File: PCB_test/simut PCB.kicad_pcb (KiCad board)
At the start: 2 copper layers, 125 x 102 mm, 49 parts, among them J1 Conn_01x10, J2 Conn_01x10, J3 Conn_01x03, J4 Conn_01x12, J5 Conn_01x14, J6 Conn_01x03, J7 Conn_01x03, Q1 BC337, U2 HLK-PM01

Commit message: Update PCB_test: refresh Gerber fabrication files and KiCad PCB layout
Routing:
- net GND: track 205.8 -> 220.7 mm

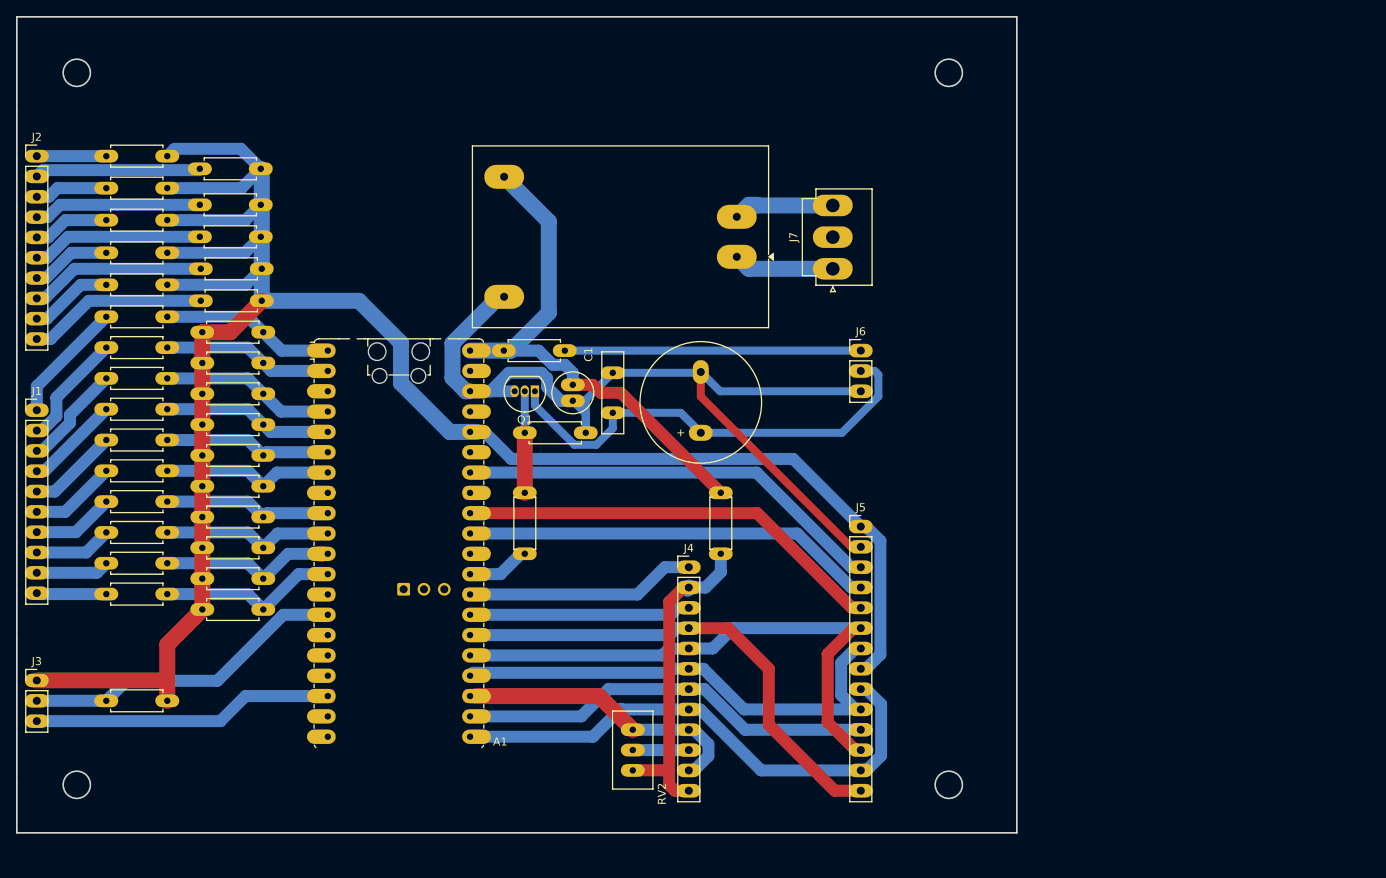
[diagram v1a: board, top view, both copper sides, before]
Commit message: Update PCB_test: correct the alphanumeric display pinout and relabel the board
The alphanumeric display header carried the wrong pinout. This regenerates the
layout and the whole fabrication output from it, so the Gerbers, the drill files
and the zip all come from the same source revision as the .kicad_pcb.

The silkscreen went from three stray numbers to a labelled board: pin names for
the TFT and touch headers, the HD44780 block under an "Alphanumeric" caption,
the sensor column S0 to S10, the mains warning and the project URL. Copper zones
were refilled as a consequence, which is most of the diff size.

The zip carries the ten fabrication files plus the .kicad_pcb source, and every
file in it is byte-identical to its loose copy in this directory.
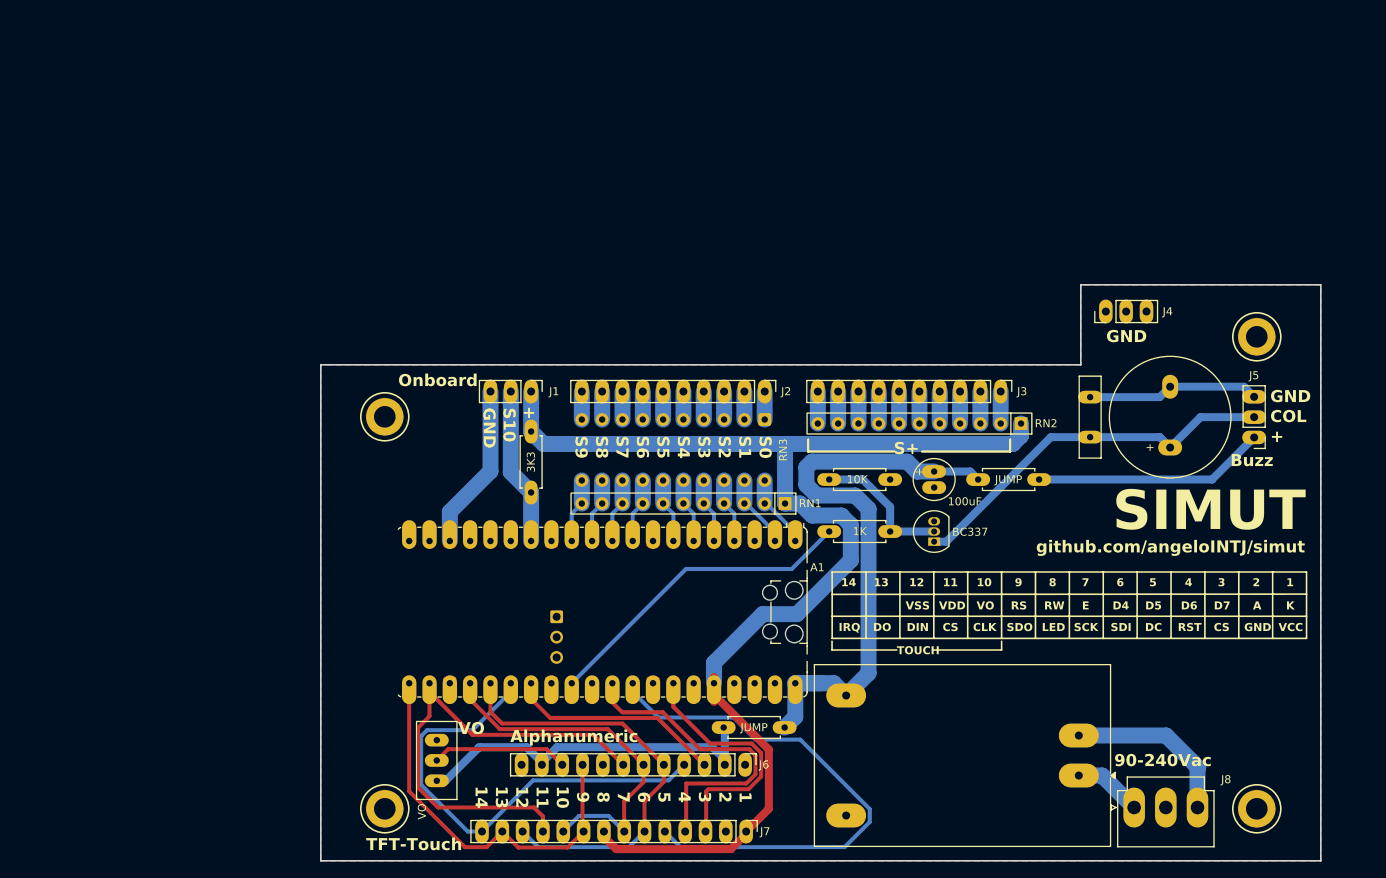
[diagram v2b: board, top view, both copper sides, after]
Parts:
- removed R1, R10, R11, R12, R13, R14, R15, R16, R17, R18, R19, R2, R20, R21, R22, R23, R24, R25, R26, R27, R28, R29, R3, R30, R4, R5, R6, R7, R8, R9: R, Resistor_THT:R_Axial_DIN0207_L6.3mm_D2.5mm_P7.62mm_Horizontal
- added J4: Conn_01x03, Connector_PinHeader_2.54mm:PinHeader_1x03_P2.54mm_Vertical, F.Cu at (183.1, 61.3)
- added REF**: MountingHole_2.7mm_M2.5_DIN965_Pad, MountingHole:MountingHole_2.7mm_M2.5_DIN965_Pad, F.Cu at (202.0, 123.5)
- added REF**: MountingHole_2.7mm_M2.5_DIN965_Pad, MountingHole:MountingHole_2.7mm_M2.5_DIN965_Pad, F.Cu at (93.0, 123.5)
- added REF**: MountingHole_2.7mm_M2.5_DIN965_Pad, MountingHole:MountingHole_2.7mm_M2.5_DIN965_Pad, F.Cu at (202.0, 64.5)
- added REF**: MountingHole_2.7mm_M2.5_DIN965_Pad, MountingHole:MountingHole_2.7mm_M2.5_DIN965_Pad, F.Cu at (93.0, 74.5)
- added RN1: R_Network10, Resistor_THT:R_Array_SIP11, F.Cu at (143.0, 85.3)
- added RN2: R_Network10, Resistor_THT:R_Array_SIP11, F.Cu at (172.5, 75.3)
- added RN3: R_Pack10, Package_DIP:DIP-20_W7.62mm, F.Cu at (140.5, 74.8)
- moved J3 124.0 mm to (170.0, 71.3), turned to -90 degrees
- moved J2 91.0 mm to (140.5, 71.3), turned to -90 degrees
- moved U2 77.7 mm to (179.8, 119.3)
- moved J8 77.2 mm to (186.7, 123.3), turned to 0 degrees
- moved J1 71.6 mm to (111.3, 71.3), turned to -90 degrees
- moved R35 61.4 mm to (167.2, 82.3)
- moved C2 59.7 mm to (181.2, 77.0)
- moved BZ1 58.7 mm to (191.2, 78.3)
- moved R31 56.6 mm to (111.3, 76.3), turned to -90 degrees
- moved BC337 53.3 mm to (161.7, 90.1), turned to 90 degrees
- moved J5 50.4 mm to (201.7, 77.1), turned to 180 degrees
- moved 100uF 46.5 mm to (161.7, 81.3)
- moved J7 40.7 mm to (138.2, 126.3), turned to -90 degrees
- moved R34 38.5 mm to (148.6, 82.3)
- moved R33 38.2 mm to (148.6, 88.8), turned to 0 degrees
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- renumbered C1 to 100uF, Q1 to BC337, J3 to J1, J1 to J2, J2 to J3, J6 to J5, J4 to J6, J5 to J7, J7 to J8, RV2 to VO
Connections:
- J6 pad 11: GND -> Net-(J4-Pin_12)
- J6 pad 12: Net-(J4-Pin_12) -> GND
- J6 pad 8: Net-(A1-GPIO16) -> GND
- J6 pad 9: GND -> Net-(A1-GPIO16)
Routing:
- net GND: track 220.7 -> 44.0 mm
- net VDD: track 265.8 -> 162.6 mm
- net Net-(A1-GPIO22): track 7.39 -> 40.8 mm
- net Net-(A1-GPIO10): track 40.8 -> 19.7 mm
- net Net-(A1-GPIO28_ADC2): track 53.7 -> 33.6 mm
- net Net-(A1-GPIO16): track 67.8 -> 48.3 mm
- net Net-(J2-Pin_10): track 22.5 -> 4.00 mm
- net Net-(A1-GPIO18): track 63.0 -> 44.9 mm
- net Net-(J2-Pin_8): track 22.0 -> 4.00 mm
- net Net-(J2-Pin_6): track 21.5 -> 4.00 mm
- net Net-(J2-Pin_4): track 21.0 -> 4.00 mm
- net Net-(J2-Pin_2): track 20.8 -> 4.00 mm
- net Net-(A1-GPIO19): track 70.7 -> 54.2 mm
- net Net-(A1-GPIO9): track 22.7 -> 8.09 mm
- net Net-(A1-GPIO27_ADC1): track 52.9 -> 67.5 mm
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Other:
- board size 125 x 102 mm -> 125 x 72 mm
- board text added: "+"
- board text added: "1"
- board text added: "10"
- board text added: "11"
- board text added: "12"
- board text added: "13"
- board text added: "14"
- board text added: "2"
- board text added: "3"
- board text added: "4"
- board text added: "5"
- board text added: "6"
- board text added: "7"
- board text added: "8"
- board text added: "9"
- board text added: "90-240Vac"
- board text added: "A"
- board text added: "Alphanumeric"
- board text added: "Buzz"
- board text added: "CLK"
- board text added: "COL"
- board text added: "CS"
- board text added: "D4"
- board text added: "D5"
- board text added: "D6"
- board text added: "D7"
- board text added: "DC"
- board text added: "DIN"
- board text added: "DO"
- board text added: "E"
- board text added: "GND"
- board text added: "IRQ"
- board text added: "K"
- board text added: "LED"
- board text added: "Onboard"
- board text added: "RS"
- board text added: "RST"
- board text added: "RW"
- board text added: "S+"
- board text added: "S0"
- board text added: "S1"
- board text added: "S10"
- board text added: "S2"
- board text added: "S3"
- board text added: "S4"
- board text added: "S5"
- board text added: "S6"
- board text added: "S7"
- board text added: "S8"
- board text added: "S9"
- board text added: "SCK"
- board text added: "SDI"
- board text added: "SDO"
- board text added: "TFT-Touch"
- board text added: "TOUCH"
- board text added: "VCC"
- board text added: "VDD"
- board text added: "VO"
- board text added: "VSS"
- board text added: "github.com/angeloINTJ/simut"
